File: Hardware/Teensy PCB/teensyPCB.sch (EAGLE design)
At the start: 31 parts, among them U2 USD-SOCKETNEW

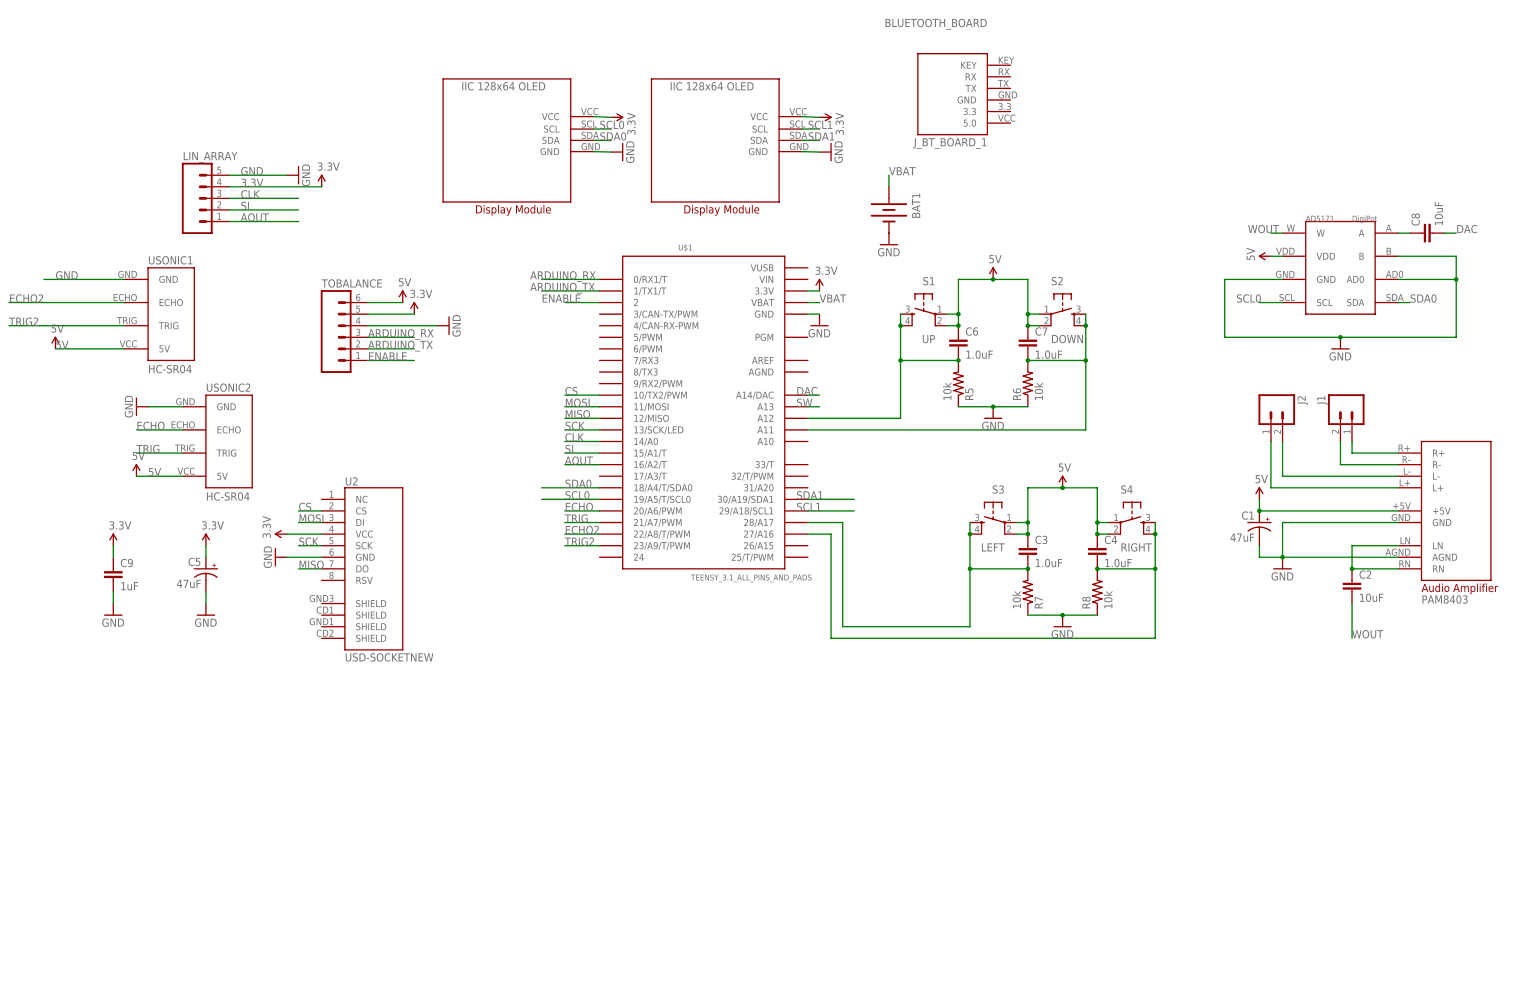
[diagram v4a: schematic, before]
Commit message: fixed HC-05 text and added leds
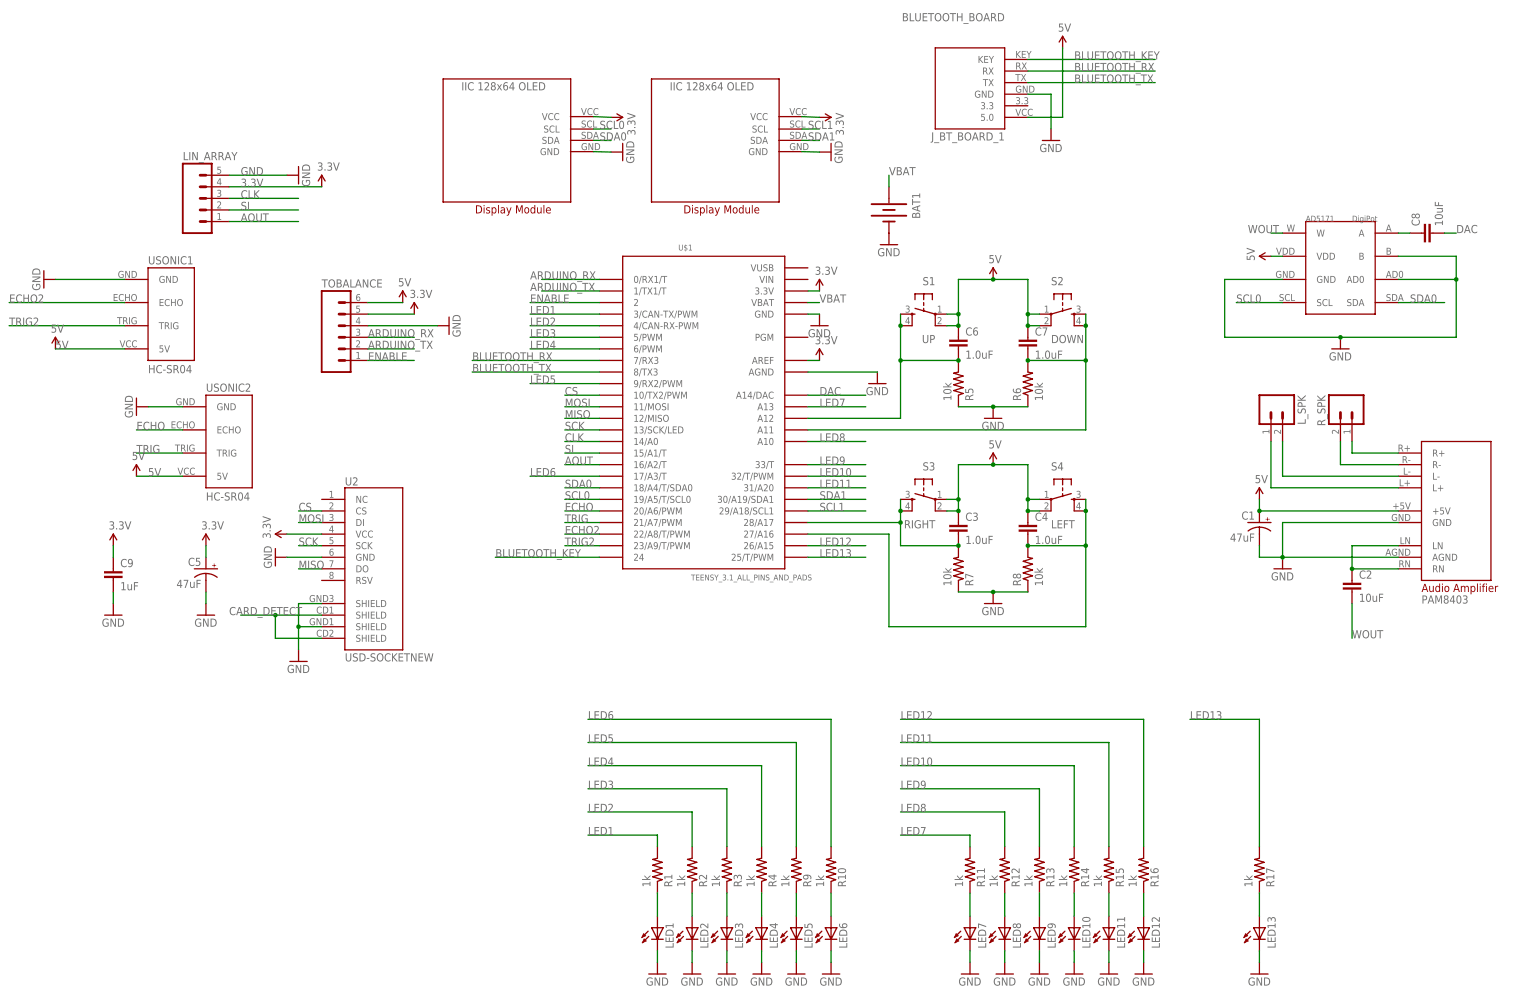
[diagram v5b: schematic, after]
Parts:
- added LED1, LED10, LED11, LED12, LED13, LED2, LED3, LED4, LED5, LED6, LED7, LED8, LED9: (no value), adafruit:LEDCHIP-LED0805
- added R1, R10, R11, R12, R13, R14, R15, R16, R17, R2, R3, R4, R9: 1k, SparkFun-Resistors:RESISTOR0805-RES
- S3: value LEFT -> RIGHT
- S4: value RIGHT -> LEFT
- renumbered J1 to R_SPK, J2 to L_SPK
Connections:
- removed net SW: U$1.A13
- new net BLUETOOTH_KEY: J_BT_BOARD_1.KEY, U$1.24
- new net BLUETOOTH_RX: J_BT_BOARD_1.RX, U$1.7/RX3
- new net BLUETOOTH_TX: J_BT_BOARD_1.TX, U$1.8/TX3
- new net CARD_DETECT: U2.SHIELD@2, U2.SHIELD@4
- new net LED1: R1.2, U$1.3/CAN-TX/PWM
- new net LED10: R14.2, U$1.32/T/PWM
- new net LED11: R15.2, U$1.31/A20
- new net LED12: R16.2, U$1.26/A15
- new net LED13: R17.2, U$1.25/T/PWM
- new net LED2: R2.2, U$1.4/CAN-RX-PWM
- new net LED3: R3.2, U$1.5/PWM
- new net LED4: R4.2, U$1.6/PWM
- new net LED5: R9.2, U$1.9/RX2/PWM
- new net LED6: R10.2, U$1.17/A3/T
- new net LED7: R11.2, U$1.A13
- new net LED8: R12.2, U$1.A10
- new net LED9: R13.2, U$1.33/T
- new net N$11: LED1.A, R1.1
- new net N$12: LED2.A, R2.1
- new net N$13: LED3.A, R3.1
- new net N$14: LED4.A, R4.1
- new net N$15: LED5.A, R9.1
- new net N$16: LED6.A, R10.1
- new net N$17: LED7.A, R11.1
- new net N$18: LED8.A, R12.1
- new net N$19: LED9.A, R13.1
- new net N$20: LED10.A, R14.1
- new net N$21: LED11.A, R15.1
- new net N$22: LED12.A, R16.1
- new net N$23: LED13.A, R17.1
- net 3.3V: now also U$1.AREF
- net 5V: now also J_BT_BOARD_1.5.0
- net GND: now also J_BT_BOARD_1.GND, LED1.C, LED10.C, LED11.C, LED12.C, LED13.C, LED2.C, LED3.C, LED4.C, LED5.C, LED6.C, LED7.C, LED8.C, LED9.C, U$1.AGND, U2.SHIELD@1, U2.SHIELD@3
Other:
- moved on the sheet: C3, C4, J_BT_BOARD_1, R7, R8, S3, S4

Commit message: fixed 5V connected to buttons
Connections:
- net 3.3V: now also C3.1, C4.1, C6.1, C7.1, S1.1, S1.2, S2.1, S2.2, S3.1, S3.2, S4.1, S4.2
- net 5V: no longer C3.1, C4.1, C6.1, C7.1, S1.1, S1.2, S2.1, S2.2, S3.1, S3.2, S4.1, S4.2

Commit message: no message
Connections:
- net N$10 renamed BUTTON4
- net N$4 renamed BUTTON3
- removed net N$2: C7.2, R6.2, S2.3, S2.4, U$1.A11
- removed net N$9: C6.2, R5.2, S1.3, S1.4, U$1.A12
- new net BUTTON1: C6.2, R5.2, S1.3, S1.4, U$1.33/T
- new net BUTTON2: C7.2, R6.2, S2.3, S2.4, U$1.32/T/PWM
- net LED10: now also U$1.A11; no longer U$1.32/T/PWM
- net LED9: now also U$1.A12; no longer U$1.33/T
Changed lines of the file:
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@@
 </segment>
 </net>
-<net name="N$9" class="0">
+<net name="BUTTON1" class="0">
 <segment>
 <pinref part="S1" gate="S" pin="4"/>
@@
 <wire x1="73.66" y1="20.32" x2="60.96" y2="20.32" width="0.1524" layer="91"/>
 <wire x1="60.96" y1="20.32" x2="60.96" y2="27.94" width="0.1524" layer="91"/>
-<pinref part="U$1" gate="G$1" pin="A12"/>
-<wire x1="40.64" y1="7.62" x2="60.96" y2="7.62" width="0.1524" layer="91"/>
 <wire x1="60.96" y1="7.62" x2="60.96" y2="20.32" width="0.1524" layer="91"/>
 <junction x="60.96" y="20.32"/>
 <pinref part="C6" gate="G$1" pin="2"/>
 <junction x="73.66" y="20.32"/>
-</segment>
-</net>
-<net name="N$2" class="0">
+<label x="60.96" y="7.62" size="1.778" layer="95" rot="R90"/>
+</segment>
+<segment>
+<pinref part="U$1" gate="G$1" pin="33/T"/>
+<wire x1="40.64" y1="-2.54" x2="53.34" y2="-2.54" width="0.1524" layer="91"/>
+<label x="43.18" y="-2.54" size="1.778" layer="95"/>
+</segment>
+</net>
+<net name="BUTTON2" class="0">
 <segment>
 <pinref part="S2" gate="S" pin="4"/>
@@
 <wire x1="101.6" y1="5.08" x2="101.6" y2="20.32" width="0.1524" layer="91"/>
 <junction x="101.6" y="20.32"/>
-<pinref part="U$1" gate="G$1" pin="A11"/>
-<wire x1="40.64" y1="5.08" x2="101.6" y2="5.08" width="0.1524" layer="91"/>
 <pinref part="C7" gate="G$1" pin="2"/>
 <junction x="88.9" y="20.32"/>
+<label x="101.6" y="5.08" size="1.778" layer="95" rot="R90"/>
+</segment>
+<segment>
+<pinref part="U$1" gate="G$1" pin="32/T/PWM"/>
+<wire x1="40.64" y1="-5.08" x2="53.34" y2="-5.08" width="0.1524" layer="91"/>
+<label x="43.18" y="-5.08" size="1.778" layer="95"/>
 </segment>
 </net>
@@
 </segment>
 </net>
-<net name="N$4" class="0">
+<net name="BUTTON3" class="0">
 <segment>
 <pinref part="S3" gate="S" pin="4"/>
@@
 </segment>
 </net>
-<net name="N$10" class="0">
+<net name="BUTTON4" class="0">
 <segment>
 <pinref part="S4" gate="S" pin="4"/>
@@
 </segment>
 <segment>
-<wire x1="53.34" y1="-2.54" x2="40.64" y2="-2.54" width="0.1524" layer="91"/>
-<label x="43.18" y="-2.54" size="1.778" layer="95"/>
-<pinref part="U$1" gate="G$1" pin="33/T"/>
+<wire x1="53.34" y1="7.62" x2="40.64" y2="7.62" width="0.1524" layer="91"/>
+<label x="43.18" y="7.62" size="1.778" layer="95"/>
+<pinref part="U$1" gate="G$1" pin="A12"/>
 </segment>
 </net>
@@
 </segment>
 <segment>
-<wire x1="53.34" y1="-5.08" x2="40.64" y2="-5.08" width="0.1524" layer="91"/>
-<label x="43.18" y="-5.08" size="1.778" layer="95"/>
-<pinref part="U$1" gate="G$1" pin="32/T/PWM"/>
-</segment>
-</net>
+<wire x1="53.34" y1="5.08" x2="40.64" y2="5.08" width="0.1524" layer="91"/>
+<label x="43.18" y="5.08" size="1.778" layer="95"/>
+<pinref part="U$1" gate="G$1" pin="A11"/>
+</segment>
+</net>

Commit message: PCB finalized
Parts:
- removed C8: 10uF, SparkFun-Capacitors:1.0UF-25V-+80/-20(0805)
- added C10: 10uF, SparkFun-Capacitors:CAP_POL3528
- renumbered U2 to MICRO_SD
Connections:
- removed net N$3: C8.1, U$5.A
- new net N$2: C10.+, U$5.A
- net DAC: now also C10.-; no longer C8.2
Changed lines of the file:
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@@
 <class number="0" name="default" width="0.254" drill="0">
 </class>
-<class number="1" name="Power" width="0.4064" drill="0">
+<class number="1" name="Power" width="0.3048" drill="0">
 </class>
 </classes>
@@
 <part name="SUPPLY1" library="SparkFun-Aesthetics" deviceset="3.3V" device=""/>
 <part name="GND1" library="SparkFun-Aesthetics" deviceset="GND" device=""/>
-<part name="U2" library="SparkFun-Connectors" deviceset="USD-SOCKET" device="NEW"/>
+<part name="MICRO_SD" library="SparkFun-Connectors" deviceset="USD-SOCKET" device="NEW"/>
 <part name="TOBALANCE" library="SparkFun-Connectors" deviceset="M06" device="POLAR_LOCK"/>
 <part name="SUPPLY2" library="SparkFun-Aesthetics" deviceset="5V" device=""/>
@@
 <part name="C7" library="SparkFun-Capacitors" deviceset="1.0UF-25V-+80/-20(0805)" device="" value="1.0uF"/>
 <part name="C2" library="SparkFun-Capacitors" deviceset="1.0UF-25V-+80/-20(0805)" device="" value="10uF"/>
-<part name="C8" library="SparkFun-Capacitors" deviceset="1.0UF-25V-+80/-20(0805)" device="" value="10uF"/>
 <part name="C5" library="SparkFun-Capacitors" deviceset="CAP_POL" device="3528" value="47uF"/>
 <part name="C9" library="SparkFun-Capacitors" deviceset="1.0UF-25V-+80/-20(0805)" device="" value="1uF"/>
@@
 <part name="SUPPLY7" library="SparkFun-Aesthetics" deviceset="3.3V" device=""/>
 <part name="SUPPLY14" library="SparkFun-Aesthetics" deviceset="3.3V" device=""/>
+<part name="C10" library="SparkFun-Capacitors" deviceset="CAP_POL" device="3528" value="10uF"/>
 </parts>
 <sheets>
@@
 <instance part="SUPPLY1" gate="G$1" x="43.18" y="35.56"/>
 <instance part="GND1" gate="1" x="43.18" y="27.94"/>
-<instance part="U2" gate="G$1" x="-58.42" y="-22.86"/>
+<instance part="MICRO_SD" gate="G$1" x="-58.42" y="-22.86"/>
 <instance part="TOBALANCE" gate="G$1" x="-60.96" y="25.4"/>
 <instance part="SUPPLY2" gate="G$1" x="-48.26" y="33.02"/>
@@
 <instance part="C7" gate="G$1" x="88.9" y="22.86"/>
 <instance part="C2" gate="G$1" x="160.02" y="-30.48"/>
-<instance part="C8" gate="G$1" x="177.8" y="48.26" rot="R90"/>
 <instance part="C5" gate="G$1" x="-91.44" y="-25.4" rot="MR0"/>
 <instance part="C9" gate="G$1" x="-111.76" y="-27.94"/>
@@
 <instance part="SUPPLY7" gate="G$1" x="81.28" y="38.1"/>
 <instance part="SUPPLY14" gate="G$1" x="81.28" y="-2.54"/>
+<instance part="C10" gate="G$1" x="175.26" y="48.26" rot="MR270"/>
 </instances>
 <busses>
@@
 </segment>
 <segment>
-<pinref part="U2" gate="G$1" pin="GND"/>
+<pinref part="MICRO_SD" gate="G$1" pin="GND"/>
 <pinref part="GND4" gate="1" pin="GND"/>
 <wire x1="-66.04" y1="-22.86" x2="-73.66" y2="-22.86" width="0.1524" layer="91"/>
@@
 </segment>
 <segment>
-<pinref part="U2" gate="G$1" pin="SHIELD@1"/>
+<pinref part="MICRO_SD" gate="G$1" pin="SHIELD@1"/>
 <pinref part="GND15" gate="1" pin="GND"/>
 <wire x1="-66.04" y1="-33.02" x2="-71.12" y2="-33.02" width="0.1524" layer="91"/>
 <wire x1="-71.12" y1="-33.02" x2="-71.12" y2="-38.1" width="0.1524" layer="91"/>
-<pinref part="U2" gate="G$1" pin="SHIELD@3"/>
+<pinref part="MICRO_SD" gate="G$1" pin="SHIELD@3"/>
 <wire x1="-71.12" y1="-38.1" x2="-71.12" y2="-43.18" width="0.1524" layer="91"/>
 <wire x1="-66.04" y1="-38.1" x2="-71.12" y2="-38.1" width="0.1524" layer="91"/>
@@
 </segment>
 <segment>
-<pinref part="U2" gate="G$1" pin="VCC"/>
+<pinref part="MICRO_SD" gate="G$1" pin="VCC"/>
 <pinref part="SUPPLY4" gate="G$1" pin="3.3V"/>
 <wire x1="-66.04" y1="-17.78" x2="-73.66" y2="-17.78" width="0.1524" layer="91"/>
@@
 <net name="SCK" class="0">
 <segment>
-<pinref part="U2" gate="G$1" pin="SCK"/>
+<pinref part="MICRO_SD" gate="G$1" pin="SCK"/>
 <wire x1="-66.04" y1="-20.32" x2="-71.12" y2="-20.32" width="0.1524" layer="91"/>
 <label x="-71.12" y="-20.32" size="1.778" layer="95"/>
@@
 <net name="MISO" class="0">
 <segment>
-<pinref part="U2" gate="G$1" pin="DO"/>
+<pinref part="MICRO_SD" gate="G$1" pin="DO"/>
 <wire x1="-66.04" y1="-25.4" x2="-71.12" y2="-25.4" width="0.1524" layer="91"/>
 <label x="-71.12" y="-25.4" size="1.778" layer="95"/>
@@
 <net name="MOSI" class="0">
 <segment>
-<pinref part="U2" gate="G$1" pin="DI"/>
+<pinref part="MICRO_SD" gate="G$1" pin="DI"/>
 <wire x1="-66.04" y1="-15.24" x2="-71.12" y2="-15.24" width="0.1524" layer="91"/>
 <label x="-71.12" y="-15.24" size="1.778" layer="95"/>
@@
 </segment>
 <segment>
-<pinref part="U2" gate="G$1" pin="CS"/>
+<pinref part="MICRO_SD" gate="G$1" pin="CS"/>
 <wire x1="-66.04" y1="-12.7" x2="-71.12" y2="-12.7" width="0.1524" layer="91"/>
 <label x="-71.12" y="-12.7" size="1.778" layer="95"/>
@@
 <wire x1="180.34" y1="48.26" x2="182.88" y2="48.26" width="0.1524" layer="91"/>
 <label x="182.88" y="48.26" size="1.778" layer="95"/>
-<pinref part="C8" gate="G$1" pin="2"/>
+<pinref part="C10" gate="G$1" pin="-"/>
 </segment>
 </net>
@@
 <wire x1="40.64" y1="-5.08" x2="53.34" y2="-5.08" width="0.1524" layer="91"/>
 <label x="43.18" y="-5.08" size="1.778" layer="95"/>
-</segment>
-</net>
-<net name="N$3" class="0">
-<segment>
-<pinref part="U$5" gate="G$1" pin="A"/>
-<wire x1="170.18" y1="48.26" x2="172.72" y2="48.26" width="0.1524" layer="91"/>
-<pinref part="C8" gate="G$1" pin="1"/>
 </segment>
 </net>
@@
 <net name="CARD_DETECT" class="0">
 <segment>
-<pinref part="U2" gate="G$1" pin="SHIELD@2"/>
+<pinref part="MICRO_SD" gate="G$1" pin="SHIELD@2"/>
 <wire x1="-66.04" y1="-35.56" x2="-76.2" y2="-35.56" width="0.1524" layer="91"/>
-<pinref part="U2" gate="G$1" pin="SHIELD@4"/>
+<pinref part="MICRO_SD" gate="G$1" pin="SHIELD@4"/>
 <wire x1="-66.04" y1="-40.64" x2="-76.2" y2="-40.64" width="0.1524" layer="91"/>
 <wire x1="-76.2" y1="-40.64" x2="-76.2" y2="-35.56" width="0.1524" layer="91"/>
@@
 </segment>
 </net>
+<net name="N$2" class="0">
+<segment>
+<pinref part="U$5" gate="G$1" pin="A"/>
+<pinref part="C10" gate="G$1" pin="+"/>
+<wire x1="172.72" y1="48.26" x2="170.18" y2="48.26" width="0.1524" layer="91"/>
+</segment>
+</net>
